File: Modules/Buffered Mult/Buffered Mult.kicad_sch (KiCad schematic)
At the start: 20 parts

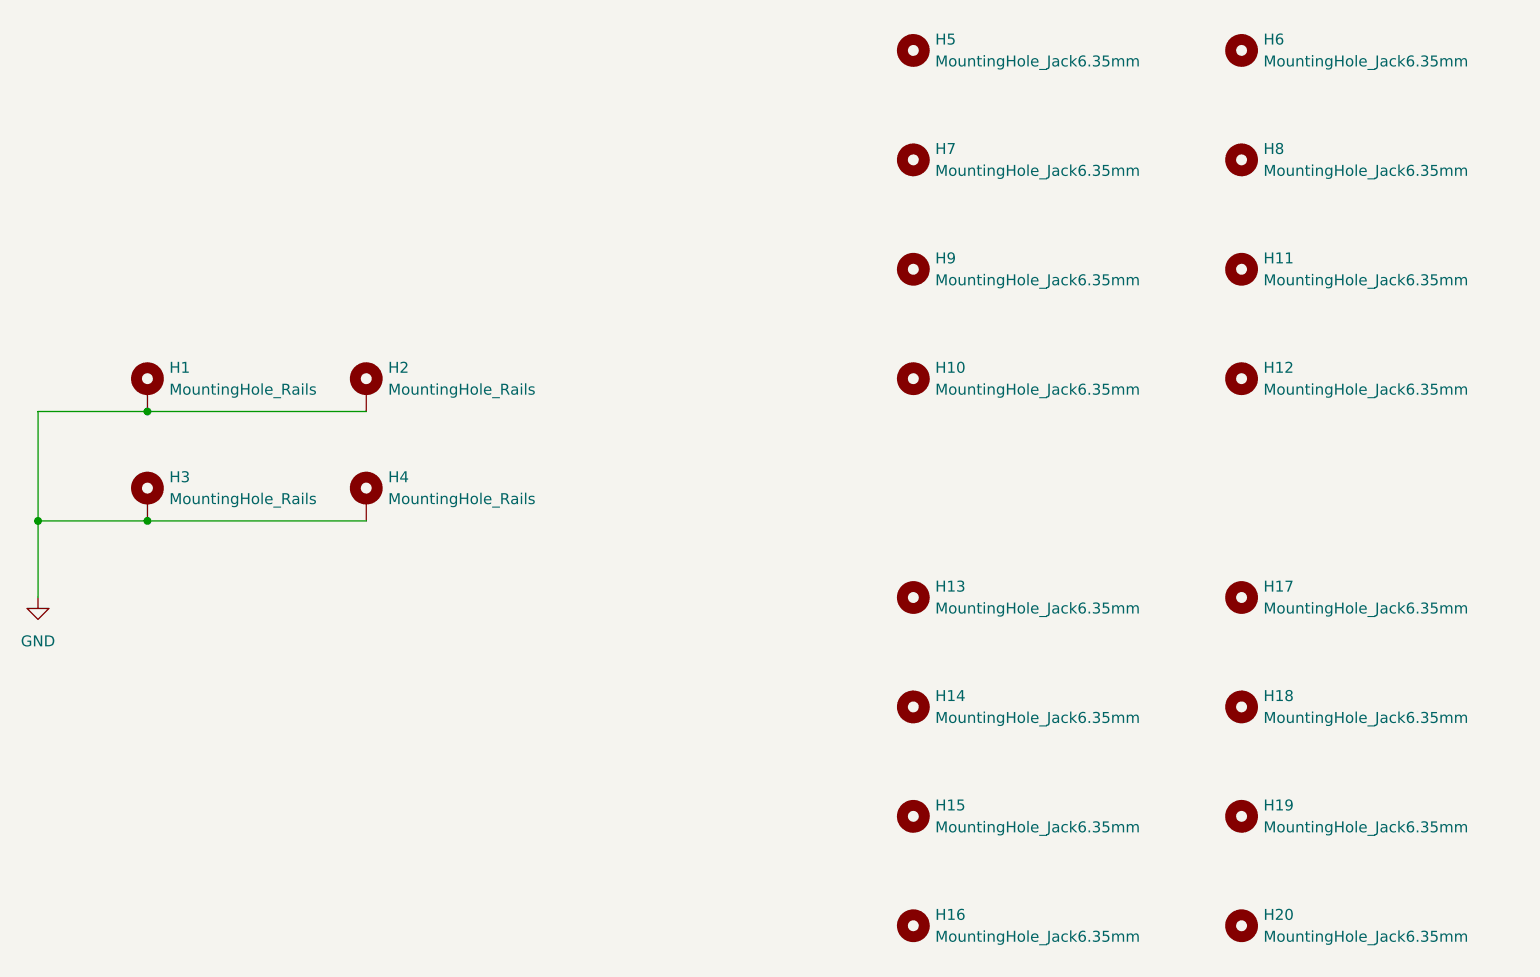
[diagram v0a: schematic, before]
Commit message: Updated jack types and decals
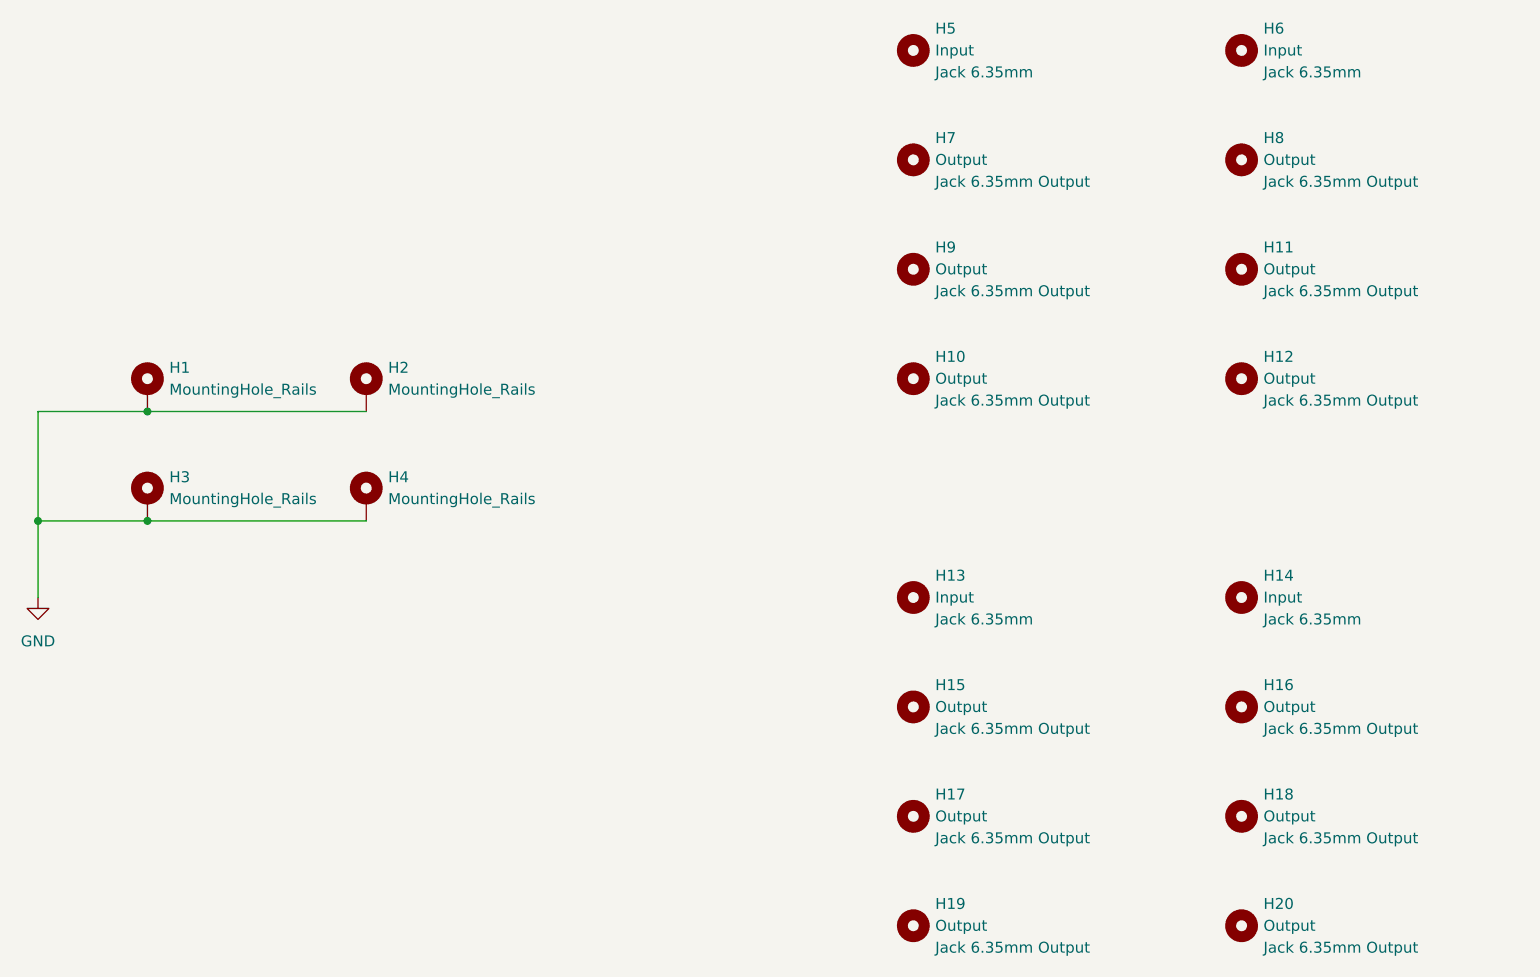
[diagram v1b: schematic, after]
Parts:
- H10, H11, H12, H15, H16, H17, H18, H19, H20, H7, H8, H9: value MountingHole_Jack6.35mm -> Output; footprint SynthStuff:Jack_6.35mm_Cutout -> SynthStuff:Jack_6.35mm_Cutout_Output; symbol SynthStuff:MountingHole_Jack6.35mm -> SynthStuff:MountingHole_Jack6.35mm_Output
- H13, H14, H5, H6: value MountingHole_Jack6.35mm -> Input
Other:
- moved on the sheet: H14, H15, H16, H17, H18, H19

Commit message: Used jack holes with edge cuts
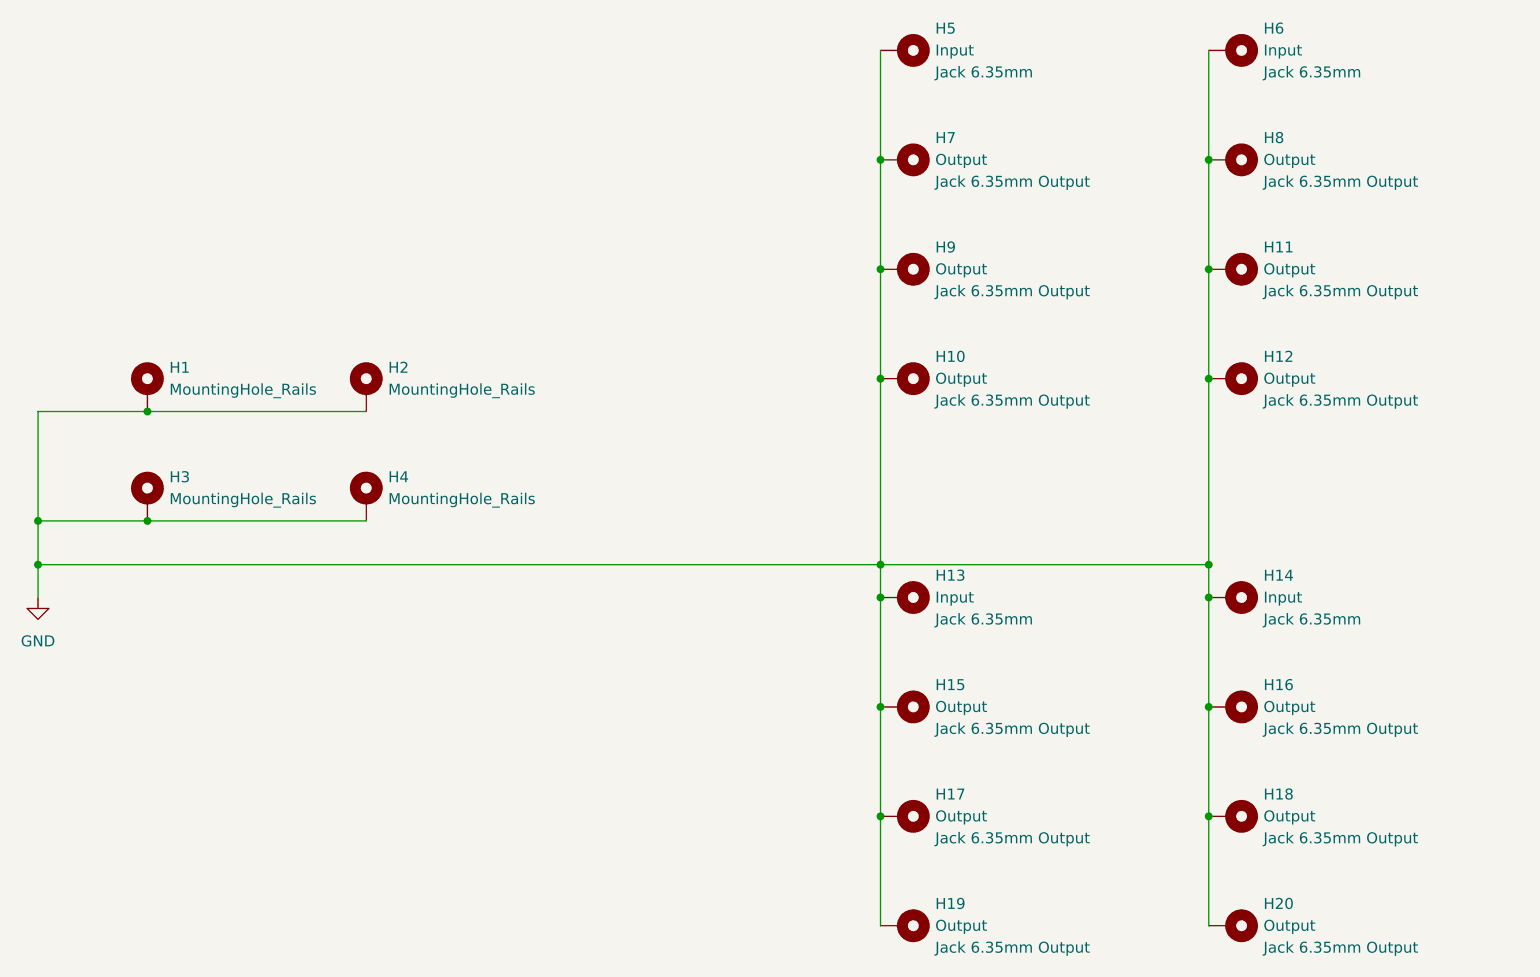
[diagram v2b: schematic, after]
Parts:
- H10, H11, H12, H15, H16, H17, H18, H19, H20, H7, H8, H9: footprint SynthStuff:Jack_6.35mm_Cutout_Output -> SynthStuff:Jack_6.35mm_Cutout_Output_v2; symbol SynthStuff:MountingHole_Jack6.35mm_Output -> SynthStuff:MountingHole_Jack6.35mm_Output_v2
- H13, H14, H5, H6: footprint SynthStuff:Jack_6.35mm_Cutout -> SynthStuff:Jack_6.35mm_Cutout_v2; symbol SynthStuff:MountingHole_Jack6.35mm -> SynthStuff:MountingHole_Jack6.35mm_v2
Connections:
- net GND: now also H10.1, H11.1, H12.1, H13.1, H14.1, H15.1, H16.1, H17.1, H18.1, H19.1, H20.1, H5.1, H6.1, H7.1, H8.1, H9.1

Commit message: Pointed to v4 output jack footprints
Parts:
- H10, H11, H12, H15, H16, H17, H18, H19, H20, H7, H8, H9: footprint SynthStuff:Jack_6.35mm_Cutout_Output_v2 -> SynthStuff:Jack_6.35mm_Cutout_Output_v4
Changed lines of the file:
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@@
 			)
 		)
-		(property "Footprint" "SynthStuff:Jack_6.35mm_Cutout_Output_v2"
+		(property "Footprint" "SynthStuff:Jack_6.35mm_Cutout_Output_v4"
 			(at 152.4 38.1 0)
 			(effects
@@
 			)
 		)
-		(property "Footprint" "SynthStuff:Jack_6.35mm_Cutout_Output_v2"
+		(property "Footprint" "SynthStuff:Jack_6.35mm_Cutout_Output_v4"
 			(at 152.4 50.8 0)
 			(effects
@@
 			)
 		)
-		(property "Footprint" "SynthStuff:Jack_6.35mm_Cutout_Output_v2"
+		(property "Footprint" "SynthStuff:Jack_6.35mm_Cutout_Output_v4"
 			(at 190.5 114.3 0)
 			(effects
@@
 			)
 		)
-		(property "Footprint" "SynthStuff:Jack_6.35mm_Cutout_Output_v2"
+		(property "Footprint" "SynthStuff:Jack_6.35mm_Cutout_Output_v4"
 			(at 152.4 101.6 0)
 			(effects
@@
 			)
 		)
-		(property "Footprint" "SynthStuff:Jack_6.35mm_Cutout_Output_v2"
+		(property "Footprint" "SynthStuff:Jack_6.35mm_Cutout_Output_v4"
 			(at 190.5 127 0)
 			(effects
@@
 			)
 		)
-		(property "Footprint" "SynthStuff:Jack_6.35mm_Cutout_Output_v2"
+		(property "Footprint" "SynthStuff:Jack_6.35mm_Cutout_Output_v4"
 			(at 190.5 63.5 0)
 			(effects
@@
 			)
 		)
-		(property "Footprint" "SynthStuff:Jack_6.35mm_Cutout_Output_v2"
+		(property "Footprint" "SynthStuff:Jack_6.35mm_Cutout_Output_v4"
 			(at 152.4 63.5 0)
 			(effects
@@
 			)
 		)
-		(property "Footprint" "SynthStuff:Jack_6.35mm_Cutout_Output_v2"
+		(property "Footprint" "SynthStuff:Jack_6.35mm_Cutout_Output_v4"
 			(at 190.5 50.8 0)
 			(effects
@@
 			)
 		)
-		(property "Footprint" "SynthStuff:Jack_6.35mm_Cutout_Output_v2"
+		(property "Footprint" "SynthStuff:Jack_6.35mm_Cutout_Output_v4"
 			(at 152.4 114.3 0)
 			(effects
@@
 			)
 		)
-		(property "Footprint" "SynthStuff:Jack_6.35mm_Cutout_Output_v2"
+		(property "Footprint" "SynthStuff:Jack_6.35mm_Cutout_Output_v4"
 			(at 190.5 38.1 0)
 			(effects
@@
 			)
 		)
-		(property "Footprint" "SynthStuff:Jack_6.35mm_Cutout_Output_v2"
+		(property "Footprint" "SynthStuff:Jack_6.35mm_Cutout_Output_v4"
 			(at 152.4 127 0)
 			(effects
@@
 			)
 		)
-		(property "Footprint" "SynthStuff:Jack_6.35mm_Cutout_Output_v2"
+		(property "Footprint" "SynthStuff:Jack_6.35mm_Cutout_Output_v4"
 			(at 190.5 101.6 0)
 			(effects

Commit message: Used jack cutout v5
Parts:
- H10, H11, H12, H15, H16, H17, H18, H19, H20, H7, H8, H9: footprint SynthStuff:Jack_6.35mm_Cutout_Output_v4 -> SynthStuff:Jack_6.35mm_Cutout_Output_v5
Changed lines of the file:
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@@
 			)
 		)
-		(property "Footprint" "SynthStuff:Jack_6.35mm_Cutout_Output_v4"
+		(property "Footprint" "SynthStuff:Jack_6.35mm_Cutout_Output_v5"
 			(at 152.4 38.1 0)
 			(effects
@@
 			)
 		)
-		(property "Footprint" "SynthStuff:Jack_6.35mm_Cutout_Output_v4"
+		(property "Footprint" "SynthStuff:Jack_6.35mm_Cutout_Output_v5"
 			(at 152.4 50.8 0)
 			(effects
@@
 			)
 		)
-		(property "Footprint" "SynthStuff:Jack_6.35mm_Cutout_Output_v4"
+		(property "Footprint" "SynthStuff:Jack_6.35mm_Cutout_Output_v5"
 			(at 190.5 114.3 0)
 			(effects
@@
 			)
 		)
-		(property "Footprint" "SynthStuff:Jack_6.35mm_Cutout_Output_v4"
+		(property "Footprint" "SynthStuff:Jack_6.35mm_Cutout_Output_v5"
 			(at 152.4 101.6 0)
 			(effects
@@
 			)
 		)
-		(property "Footprint" "SynthStuff:Jack_6.35mm_Cutout_Output_v4"
+		(property "Footprint" "SynthStuff:Jack_6.35mm_Cutout_Output_v5"
 			(at 190.5 127 0)
 			(effects
@@
 			)
 		)
-		(property "Footprint" "SynthStuff:Jack_6.35mm_Cutout_Output_v4"
+		(property "Footprint" "SynthStuff:Jack_6.35mm_Cutout_Output_v5"
 			(at 190.5 63.5 0)
 			(effects
@@
 			)
 		)
-		(property "Footprint" "SynthStuff:Jack_6.35mm_Cutout_Output_v4"
+		(property "Footprint" "SynthStuff:Jack_6.35mm_Cutout_Output_v5"
 			(at 152.4 63.5 0)
 			(effects
@@
 			)
 		)
-		(property "Footprint" "SynthStuff:Jack_6.35mm_Cutout_Output_v4"
+		(property "Footprint" "SynthStuff:Jack_6.35mm_Cutout_Output_v5"
 			(at 190.5 50.8 0)
 			(effects
@@
 			)
 		)
-		(property "Footprint" "SynthStuff:Jack_6.35mm_Cutout_Output_v4"
+		(property "Footprint" "SynthStuff:Jack_6.35mm_Cutout_Output_v5"
 			(at 152.4 114.3 0)
 			(effects
@@
 			)
 		)
-		(property "Footprint" "SynthStuff:Jack_6.35mm_Cutout_Output_v4"
+		(property "Footprint" "SynthStuff:Jack_6.35mm_Cutout_Output_v5"
 			(at 190.5 38.1 0)
 			(effects
@@
 			)
 		)
-		(property "Footprint" "SynthStuff:Jack_6.35mm_Cutout_Output_v4"
+		(property "Footprint" "SynthStuff:Jack_6.35mm_Cutout_Output_v5"
 			(at 152.4 127 0)
 			(effects
@@
 			)
 		)
-		(property "Footprint" "SynthStuff:Jack_6.35mm_Cutout_Output_v4"
+		(property "Footprint" "SynthStuff:Jack_6.35mm_Cutout_Output_v5"
 			(at 190.5 101.6 0)
 			(effects

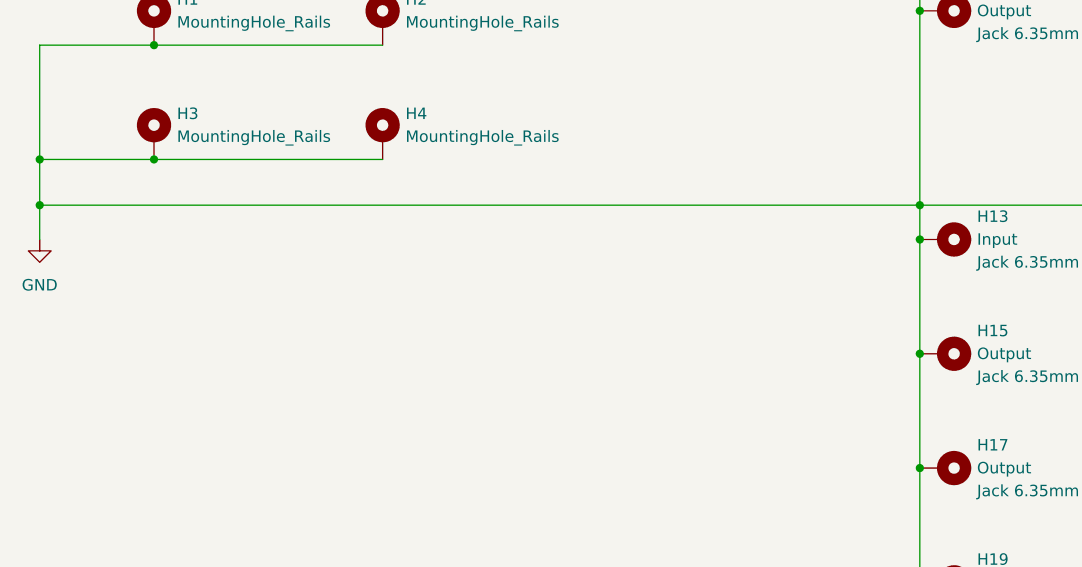
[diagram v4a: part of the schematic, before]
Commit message: Added 0V solder pad and pin to panel and PCB
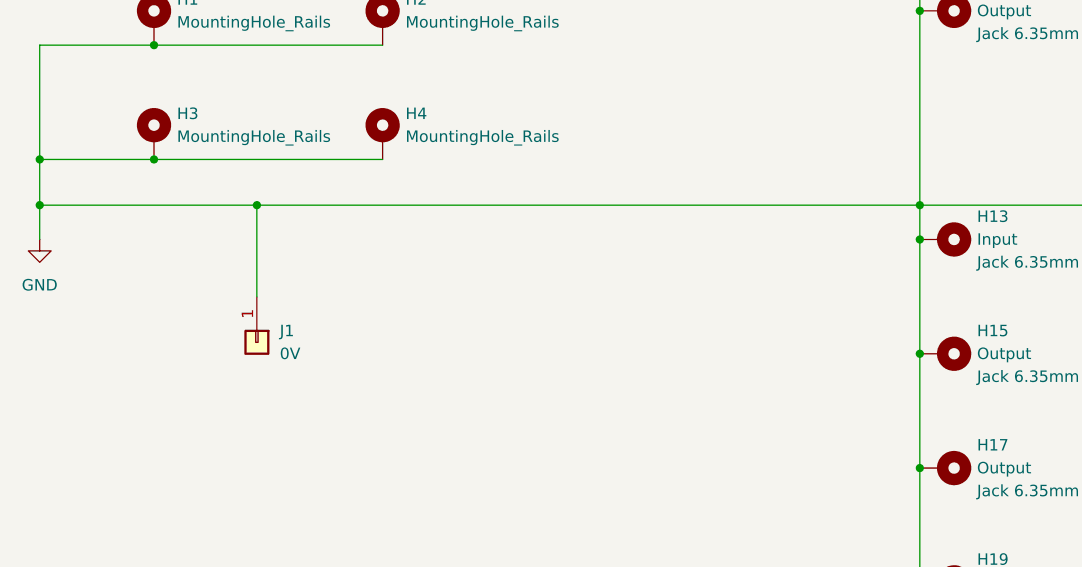
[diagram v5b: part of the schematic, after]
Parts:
- added J1: 0V, Connector_Wire:SolderWirePad_1x01_SMD_5x10mm, symbol Connector_Generic:Conn_01x01
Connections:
- net GND: now also J1.1 (Pin_1)
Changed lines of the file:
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@@
+	)
+	(junction
+		(at 74.93 85.09)
+		(diameter 0)
+		(color 0 0 0 0)
 	)
 	(junction
@@
 	(wire
 		(pts
-			(xy 50.8 85.09) (xy 148.59 85.09)
+			(xy 50.8 85.09) (xy 74.93 85.09)
+		)
+		(stroke
+			(width 0)
+			(type default)
+		)
+	)
+	(wire
+		(pts
+			(xy 74.93 85.09) (xy 148.59 85.09)
 		)
 		(stroke
@@
 		(pts
 			(xy 148.59 101.6) (xy 148.59 114.3)
+		)
+		(stroke
+			(width 0)
+			(type default)
+		)
+	)
+	(wire
+		(pts
+			(xy 74.93 85.09) (xy 74.93 95.25)
 		)
 		(stroke
@@
 					(unit 1)
 				)
+			)
+		)
+	)
+	(symbol
+		(lib_id "Connector_Generic:Conn_01x01")
+		(at 74.93 100.33 270)
+		(unit 1)
+		(exclude_from_sim no)
+		(in_bom yes)
+		(on_board yes)
+		(dnp no)
+		(fields_autoplaced yes)
+		(property "Reference" "J1"
+			(at 77.47 99.0599 90)
+			(effects
+				(font
+					(size 1.27 1.27)
+				)
+				(justify left)
+			)
+		)
+		(property "Value" "0V"
+			(at 77.47 101.5999 90)
+			(effects
+				(font
+					(size 1.27 1.27)
+				)
+				(justify left)
+			)
+		)
+		(property "Footprint" "Connector_Wire:SolderWirePad_1x01_SMD_5x10mm"
+			(at 74.93 100.33 0)
+			(effects
+				(font
+					(size 1.27 1.27)
+				)
+				(hide yes)
+			)
+		)
+		(property "Datasheet" "~"
+			(at 74.93 100.33 0)
+			(effects
+				(font
+					(size 1.27 1.27)
+				)
+				(hide yes)
+			)
+		)
+		(property "Description" "Generic connector, single row, 01x01, script generated (kicad-library-utils/schlib/autogen/connector/)"
+			(at 74.93 100.33 0)
+			(effects
+				(font
+					(size 1.27 1.27)
+				)
+				(hide yes)
+			)
+		)
+		(pin "1"
+		)
+		(instances
+			(project ""
+				(path "/23c91e78-a36c-4491-bf34-685d390339fc"
+					(reference "J1")
+					(unit 1)
+				)
